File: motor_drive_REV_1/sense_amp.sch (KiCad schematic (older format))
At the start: 6 parts, among them U9 AD8418ABRMZ-RL

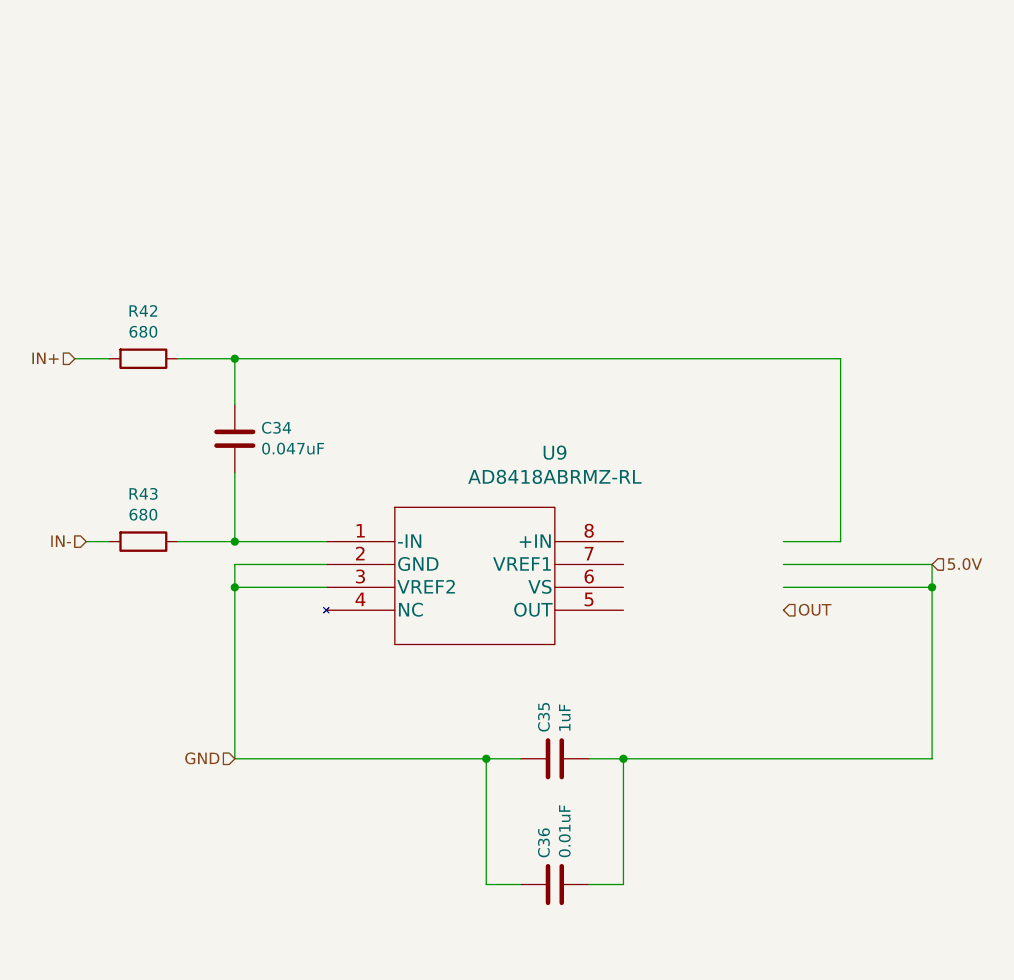
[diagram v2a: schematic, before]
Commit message: working on adding thermistors but encountered too many hierarchicaly copies bug
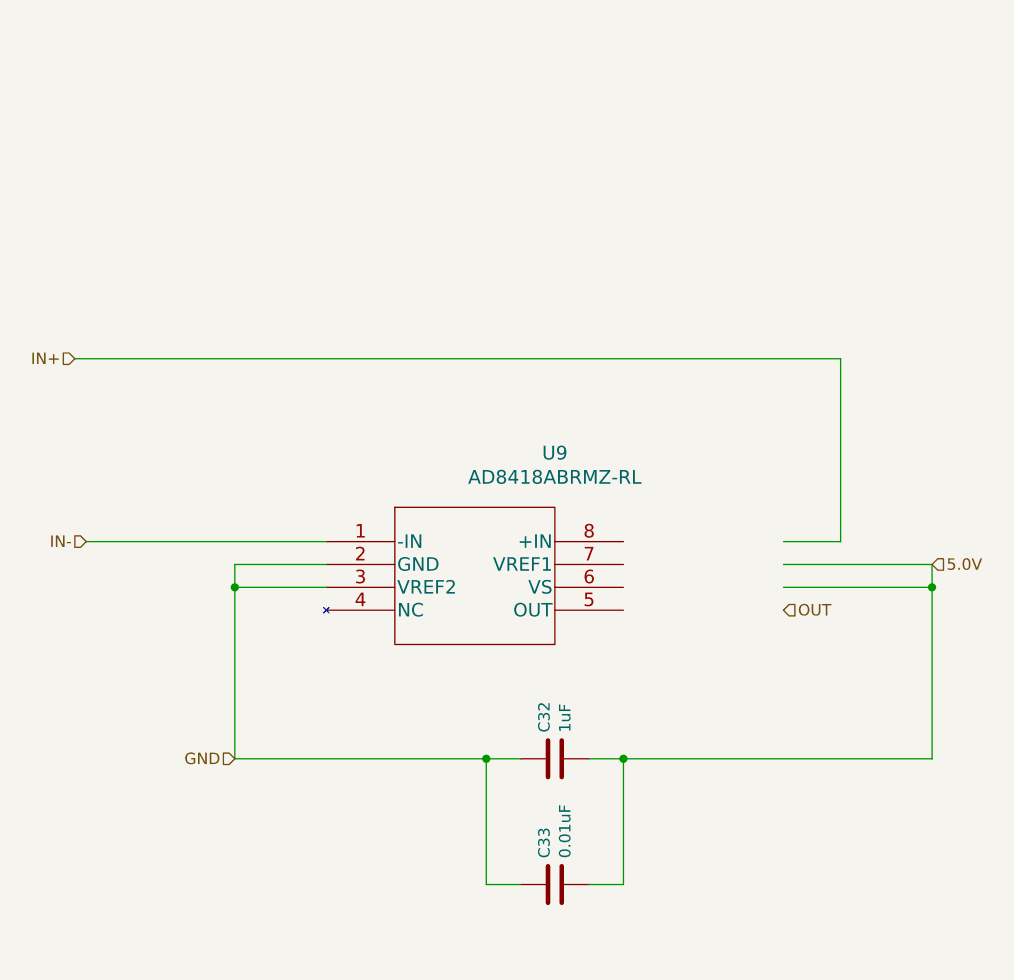
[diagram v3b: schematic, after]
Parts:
- removed C1: 0.047uF, motor_drive_footprints:C_0603_1608Metric, symbol motor_drive:C
- removed R10, R11: 680, motor_drive_footprints:C_0603_1608Metric, symbol motor_drive:R
- renumbered C35 to C32, C36 to C33
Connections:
- wire segments 26 -> 20
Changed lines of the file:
@@
 $Descr A4 11693 8268
 encoding utf-8
-Sheet 14 14
+Sheet 5 14
 Title ""
 Date ""
@@
 AR Path="/5E285F18/5E25CC80" Ref="C?"  Part="1"
 AR Path="/5E286BCF/5E25CC80" Ref="C?"  Part="1"
-AR Path="/5E291A12/5E25CC80" Ref="C35"  Part="1"
-AR Path="/5E2938C8/5E25CC80" Ref="C2"  Part="1"
+AR Path="/5E291A12/5E25CC80" Ref="C32"  Part="1"
+AR Path="/5E2938C8/5E25CC80" Ref="C3"  Part="1"
 AR Path="/5E295828/5E25CC80" Ref="C5"  Part="1"
 AR Path="/5E2E3D6E/5E25CC80" Ref="C?"  Part="1"
 AR Path="/5E2E5BBE/5E25CC80" Ref="C?"  Part="1"
 AR Path="/5E2E7F62/5E25CC80" Ref="C?"  Part="1"
-AR Path="/5E336639/5E25CC80" Ref="C8"  Part="1"
-AR Path="/5E33A08D/5E25CC80" Ref="C11"  Part="1"
+AR Path="/5E336639/5E25CC80" Ref="C7"  Part="1"
+AR Path="/5E33A08D/5E25CC80" Ref="C9"  Part="1"
 AR Path="/5E33E36D/5E25CC80" Ref="C?"  Part="1"
-F 0 "C35" H 5615 4496 50  0000 L CNN
+F 0 "C32" H 5615 4496 50  0000 L CNN
 F 1 "1uF" H 5615 4405 50  0000 L CNN
 F 2 "motor_drive_footprints:C_0603_1608Metric" H 5538 4300 50  0001 C CNN
@@
 AR Path="/5E285F18/5E3A2D2D" Ref="C?"  Part="1"
 AR Path="/5E286BCF/5E3A2D2D" Ref="C?"  Part="1"
-AR Path="/5E291A12/5E3A2D2D" Ref="C36"  Part="1"
-AR Path="/5E2938C8/5E3A2D2D" Ref="C3"  Part="1"
+AR Path="/5E291A12/5E3A2D2D" Ref="C33"  Part="1"
+AR Path="/5E2938C8/5E3A2D2D" Ref="C4"  Part="1"
 AR Path="/5E295828/5E3A2D2D" Ref="C6"  Part="1"
 AR Path="/5E2E3D6E/5E3A2D2D" Ref="C?"  Part="1"
 AR Path="/5E2E5BBE/5E3A2D2D" Ref="C?"  Part="1"
 AR Path="/5E2E7F62/5E3A2D2D" Ref="C?"  Part="1"
-AR Path="/5E336639/5E3A2D2D" Ref="C9"  Part="1"
-AR Path="/5E33A08D/5E3A2D2D" Ref="C12"  Part="1"
+AR Path="/5E336639/5E3A2D2D" Ref="C8"  Part="1"
+AR Path="/5E33A08D/5E3A2D2D" Ref="C10"  Part="1"
 AR Path="/5E33E36D/5E3A2D2D" Ref="C?"  Part="1"
-F 0 "C36" H 5615 5046 50  0000 L CNN
+F 0 "C33" H 5615 5046 50  0000 L CNN
 F 1 "0.01uF" H 5615 4955 50  0000 L CNN
 F 2 "motor_drive_footprints:C_0603_1608Metric" H 5538 4850 50  0001 C CNN
@@
 Text HLabel 3450 3500 0    50   Input ~ 0
 IN-
-$Comp
-L motor_drive:R R?
-U 1 1 5E3B6CAC
-P 3700 2700
-AR Path="/5E26944C/5E3B6CAC" Ref="R?"  Part="1"
-AR Path="/5E3B6CAC" Ref="R?"  Part="1"
-AR Path="/5E334D58/5E3B6CAC" Ref="R?"  Part="1"
-AR Path="/5E2938C8/5E3B6CAC" Ref="R10"  Part="1"
-AR Path="/5E295828/5E3B6CAC" Ref="R12"  Part="1"
-AR Path="/5E336639/5E3B6CAC" Ref="R14"  Part="1"
-AR Path="/5E33A08D/5E3B6CAC" Ref="R16"  Part="1"
-AR Path="/5E291A12/5E3B6CAC" Ref="R42"  Part="1"
-F 0 "R42" V 3493 2700 50  0000 C CNN
-F 1 "680" V 3584 2700 50  0000 C CNN
-F 2 "motor_drive_footprints:C_0603_1608Metric" V 3630 2700 50  0001 C CNN
-F 3 "~" H 3700 2700 50  0001 C CNN
-	1    3700 2700
-	0    1    1    0
-$EndComp
-$Comp
-L motor_drive:C C?
-U 1 1 5E3B79F8
-P 4100 3050
-AR Path="/5E38D632/5E3B79F8" Ref="C?"  Part="1"
-AR Path="/5E334D58/5E3B79F8" Ref="C?"  Part="1"
-AR Path="/5E2938C8/5E3B79F8" Ref="C1"  Part="1"
-AR Path="/5E295828/5E3B79F8" Ref="C4"  Part="1"
-AR Path="/5E336639/5E3B79F8" Ref="C7"  Part="1"
-AR Path="/5E33A08D/5E3B79F8" Ref="C10"  Part="1"
-AR Path="/5E291A12/5E3B79F8" Ref="C34"  Part="1"
-F 0 "C34" H 4215 3096 50  0000 L CNN
-F 1 "0.047uF" H 4215 3005 50  0000 L CNN
-F 2 "motor_drive_footprints:C_0603_1608Metric" H 4138 2900 50  0001 C CNN
-F 3 "~" H 4100 3050 50  0001 C CNN
-	1    4100 3050
-	1    0    0    -1
-$EndComp
-Wire Wire Line
-	3400 2700 3550 2700
-Wire Wire Line
-	3850 2700 4100 2700
-Wire Wire Line
-	4100 2700 6750 2700
 Wire Wire Line
 	6750 2700 6750 3500
-Connection ~ 4100 2700
 Wire Wire Line
-	4100 2700 4100 2900
+	3400 2700 6750 2700
 Wire Wire Line
-	4100 3200 4100 3500
-Wire Wire Line
-	4100 3500 4500 3500
-$Comp
-L motor_drive:R R?
-U 1 1 5E394586
-P 3700 3500
-AR Path="/5E26944C/5E394586" Ref="R?"  Part="1"
-AR Path="/5E394586" Ref="R?"  Part="1"
-AR Path="/5E334D58/5E394586" Ref="R?"  Part="1"
-AR Path="/5E2938C8/5E394586" Ref="R11"  Part="1"
-AR Path="/5E295828/5E394586" Ref="R13"  Part="1"
-AR Path="/5E336639/5E394586" Ref="R15"  Part="1"
-AR Path="/5E33A08D/5E394586" Ref="R17"  Part="1"
-AR Path="/5E291A12/5E394586" Ref="R43"  Part="1"
-F 0 "R43" V 3493 3500 50  0000 C CNN
-F 1 "680" V 3584 3500 50  0000 C CNN
-F 2 "motor_drive_footprints:C_0603_1608Metric" V 3630 3500 50  0001 C CNN
-F 3 "~" H 3700 3500 50  0001 C CNN
-	1    3700 3500
-	0    1    1    0
-$EndComp
-Wire Wire Line
-	3850 3500 4100 3500
-Connection ~ 4100 3500
-Wire Wire Line
-	3550 3500 3450 3500
+	3450 3500 4500 3500
 $EndSCHEMATC

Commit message: started layout
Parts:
- renumbered C32 to C41, C33 to C42
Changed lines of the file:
@@
 $Descr A4 11693 8268
 encoding utf-8
-Sheet 5 14
+Sheet 6 16
 Title ""
 Date ""
@@
 AR Path="/5E33A08D/5E259F13" Ref="U4"  Part="1"
 AR Path="/5E33E36D/5E259F13" Ref="U?"  Part="1"
-F 0 "U9" H 5500 3887 60  0000 C CNN
+F 0 "U2" H 5500 3887 60  0000 C CNN
 F 1 "AD8418ABRMZ-RL" H 5500 3781 60  0000 C CNN
 F 2 "motor_drive_footprints:AD8418ABRMZ-RL" H 5500 3740 60  0001 C CNN
@@
 AR Path="/5E285F18/5E25CC80" Ref="C?"  Part="1"
 AR Path="/5E286BCF/5E25CC80" Ref="C?"  Part="1"
-AR Path="/5E291A12/5E25CC80" Ref="C32"  Part="1"
-AR Path="/5E2938C8/5E25CC80" Ref="C3"  Part="1"
-AR Path="/5E295828/5E25CC80" Ref="C5"  Part="1"
+AR Path="/5E291A12/5E25CC80" Ref="C41"  Part="1"
+AR Path="/5E2938C8/5E25CC80" Ref="C1"  Part="1"
+AR Path="/5E295828/5E25CC80" Ref="C3"  Part="1"
 AR Path="/5E2E3D6E/5E25CC80" Ref="C?"  Part="1"
 AR Path="/5E2E5BBE/5E25CC80" Ref="C?"  Part="1"
 AR Path="/5E2E7F62/5E25CC80" Ref="C?"  Part="1"
-AR Path="/5E336639/5E25CC80" Ref="C7"  Part="1"
-AR Path="/5E33A08D/5E25CC80" Ref="C9"  Part="1"
+AR Path="/5E336639/5E25CC80" Ref="C5"  Part="1"
+AR Path="/5E33A08D/5E25CC80" Ref="C7"  Part="1"
 AR Path="/5E33E36D/5E25CC80" Ref="C?"  Part="1"
-F 0 "C32" H 5615 4496 50  0000 L CNN
+F 0 "C3" H 5615 4496 50  0000 L CNN
 F 1 "1uF" H 5615 4405 50  0000 L CNN
 F 2 "motor_drive_footprints:C_0603_1608Metric" H 5538 4300 50  0001 C CNN
@@
 AR Path="/5E285F18/5E3A2D2D" Ref="C?"  Part="1"
 AR Path="/5E286BCF/5E3A2D2D" Ref="C?"  Part="1"
-AR Path="/5E291A12/5E3A2D2D" Ref="C33"  Part="1"
-AR Path="/5E2938C8/5E3A2D2D" Ref="C4"  Part="1"
-AR Path="/5E295828/5E3A2D2D" Ref="C6"  Part="1"
+AR Path="/5E291A12/5E3A2D2D" Ref="C42"  Part="1"
+AR Path="/5E2938C8/5E3A2D2D" Ref="C2"  Part="1"
+AR Path="/5E295828/5E3A2D2D" Ref="C4"  Part="1"
 AR Path="/5E2E3D6E/5E3A2D2D" Ref="C?"  Part="1"
 AR Path="/5E2E5BBE/5E3A2D2D" Ref="C?"  Part="1"
 AR Path="/5E2E7F62/5E3A2D2D" Ref="C?"  Part="1"
-AR Path="/5E336639/5E3A2D2D" Ref="C8"  Part="1"
-AR Path="/5E33A08D/5E3A2D2D" Ref="C10"  Part="1"
+AR Path="/5E336639/5E3A2D2D" Ref="C6"  Part="1"
+AR Path="/5E33A08D/5E3A2D2D" Ref="C8"  Part="1"
 AR Path="/5E33E36D/5E3A2D2D" Ref="C?"  Part="1"
-F 0 "C33" H 5615 5046 50  0000 L CNN
+F 0 "C4" H 5615 5046 50  0000 L CNN
 F 1 "0.01uF" H 5615 4955 50  0000 L CNN
 F 2 "motor_drive_footprints:C_0603_1608Metric" H 5538 4850 50  0001 C CNN

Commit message: layout
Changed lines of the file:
@@
 $Descr A4 11693 8268
 encoding utf-8
-Sheet 6 16
+Sheet 14 16
 Title ""
 Date ""
@@
 AR Path="/5E33A08D/5E259F13" Ref="U4"  Part="1"
 AR Path="/5E33E36D/5E259F13" Ref="U?"  Part="1"
-F 0 "U2" H 5500 3887 60  0000 C CNN
+F 0 "U9" H 5500 3887 60  0000 C CNN
 F 1 "AD8418ABRMZ-RL" H 5500 3781 60  0000 C CNN
 F 2 "motor_drive_footprints:AD8418ABRMZ-RL" H 5500 3740 60  0001 C CNN
@@
 AR Path="/5E33A08D/5E25CC80" Ref="C7"  Part="1"
 AR Path="/5E33E36D/5E25CC80" Ref="C?"  Part="1"
-F 0 "C3" H 5615 4496 50  0000 L CNN
+F 0 "C41" H 5615 4496 50  0000 L CNN
 F 1 "1uF" H 5615 4405 50  0000 L CNN
 F 2 "motor_drive_footprints:C_0603_1608Metric" H 5538 4300 50  0001 C CNN
@@
 AR Path="/5E33A08D/5E3A2D2D" Ref="C8"  Part="1"
 AR Path="/5E33E36D/5E3A2D2D" Ref="C?"  Part="1"
-F 0 "C4" H 5615 5046 50  0000 L CNN
+F 0 "C42" H 5615 5046 50  0000 L CNN
 F 1 "0.01uF" H 5615 4955 50  0000 L CNN
 F 2 "motor_drive_footprints:C_0603_1608Metric" H 5538 4850 50  0001 C CNN

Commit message: layout
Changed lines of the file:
@@
 $Descr A4 11693 8268
 encoding utf-8
-Sheet 14 16
+Sheet 6 16
 Title ""
 Date ""
@@
 AR Path="/5E33A08D/5E259F13" Ref="U4"  Part="1"
 AR Path="/5E33E36D/5E259F13" Ref="U?"  Part="1"
-F 0 "U9" H 5500 3887 60  0000 C CNN
+F 0 "U2" H 5500 3887 60  0000 C CNN
 F 1 "AD8418ABRMZ-RL" H 5500 3781 60  0000 C CNN
 F 2 "motor_drive_footprints:AD8418ABRMZ-RL" H 5500 3740 60  0001 C CNN
@@
 AR Path="/5E33A08D/5E25CC80" Ref="C7"  Part="1"
 AR Path="/5E33E36D/5E25CC80" Ref="C?"  Part="1"
-F 0 "C41" H 5615 4496 50  0000 L CNN
+F 0 "C3" H 5615 4496 50  0000 L CNN
 F 1 "1uF" H 5615 4405 50  0000 L CNN
 F 2 "motor_drive_footprints:C_0603_1608Metric" H 5538 4300 50  0001 C CNN
@@
 AR Path="/5E33A08D/5E3A2D2D" Ref="C8"  Part="1"
 AR Path="/5E33E36D/5E3A2D2D" Ref="C?"  Part="1"
-F 0 "C42" H 5615 5046 50  0000 L CNN
+F 0 "C4" H 5615 5046 50  0000 L CNN
 F 1 "0.01uF" H 5615 4955 50  0000 L CNN
 F 2 "motor_drive_footprints:C_0603_1608Metric" H 5538 4850 50  0001 C CNN

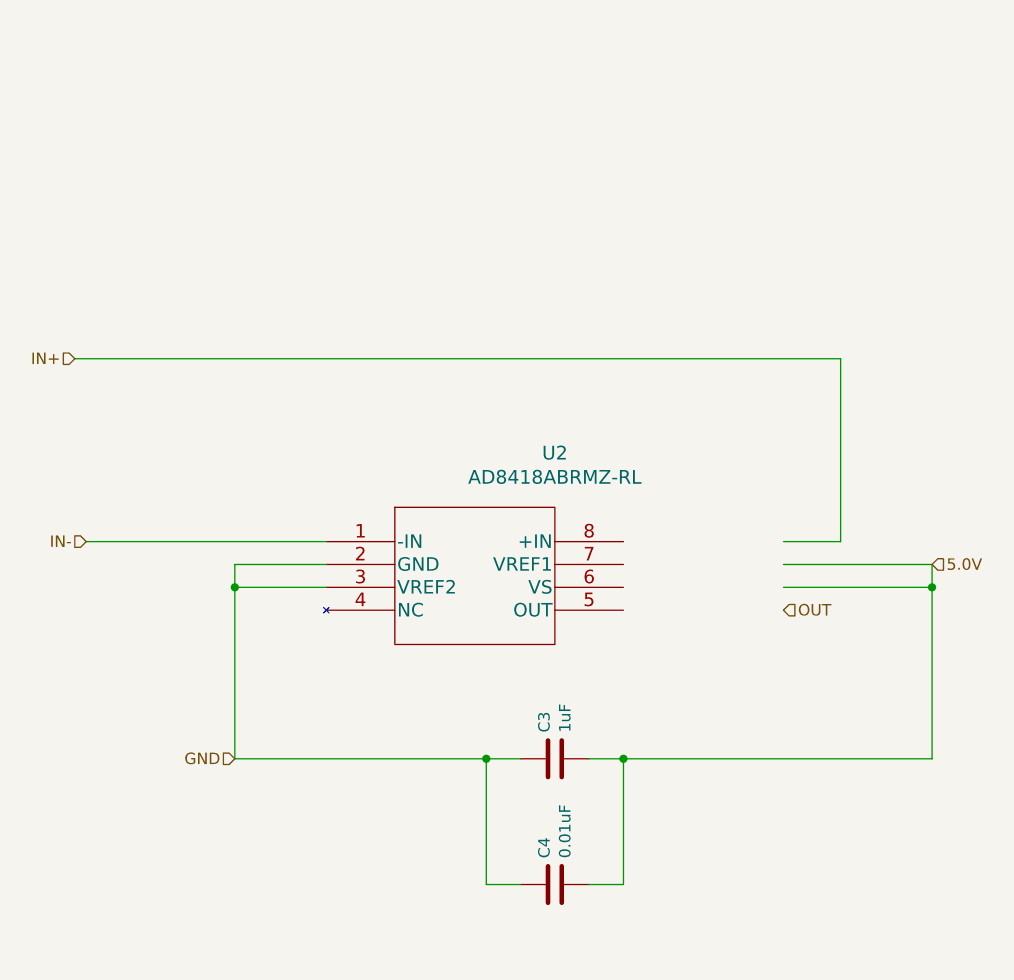
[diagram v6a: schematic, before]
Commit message: gate drive rework and schematic re-organization
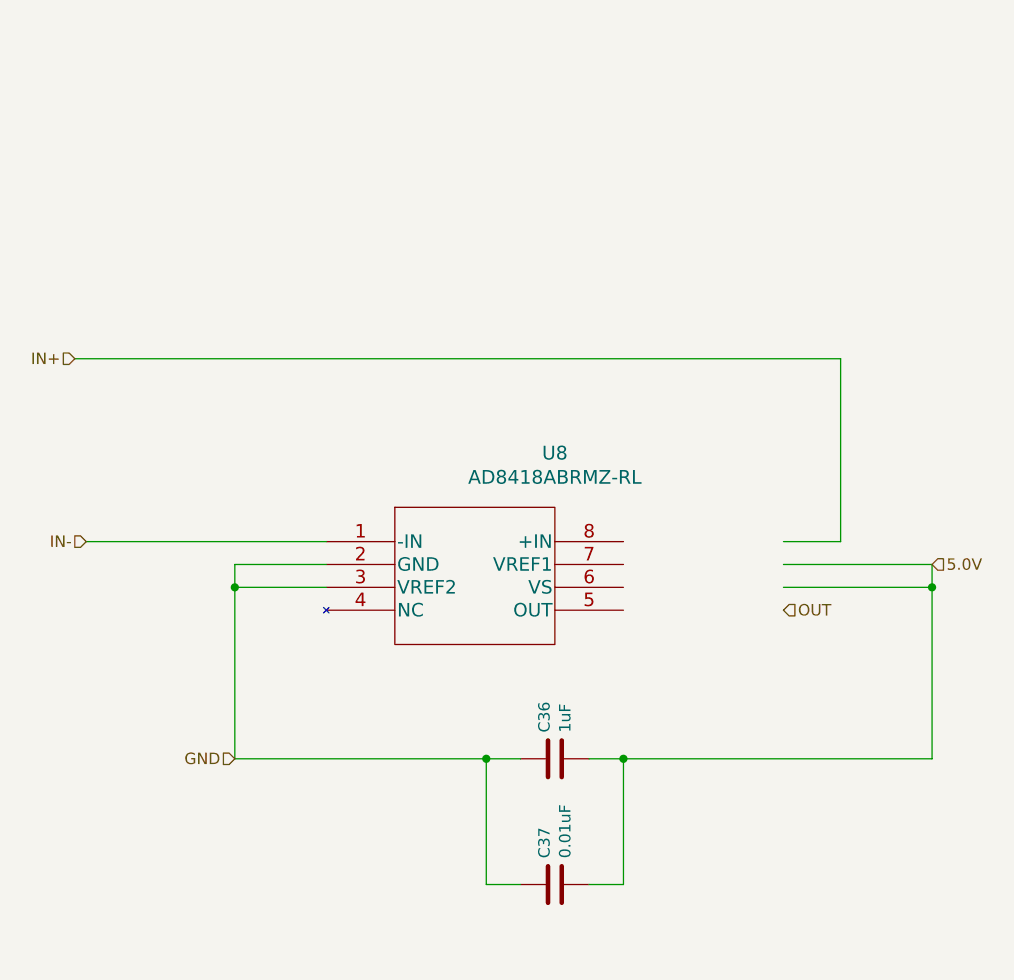
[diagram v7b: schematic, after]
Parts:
- renumbered C41 to C36, C42 to C37, U9 to U8
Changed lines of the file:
@@
 $Descr A4 11693 8268
 encoding utf-8
-Sheet 6 16
+Sheet 10 15
 Title ""
 Date ""
@@
 IN+
 $Comp
-L motor_drive:AD8418ABRMZ-RL U9
+L motor_drive:AD8418ABRMZ-RL U8
 U 1 1 5E259F13
 P 4500 3500
-AR Path="/5E291A12/5E259F13" Ref="U9"  Part="1"
+AR Path="/5E291A12/5E259F13" Ref="U8"  Part="1"
 AR Path="/5E2938C8/5E259F13" Ref="U1"  Part="1"
 AR Path="/5E295828/5E259F13" Ref="U2"  Part="1"
@@
 AR Path="/5E33A08D/5E259F13" Ref="U4"  Part="1"
 AR Path="/5E33E36D/5E259F13" Ref="U?"  Part="1"
-F 0 "U2" H 5500 3887 60  0000 C CNN
+F 0 "U8" H 5500 3887 60  0000 C CNN
 F 1 "AD8418ABRMZ-RL" H 5500 3781 60  0000 C CNN
 F 2 "motor_drive_footprints:AD8418ABRMZ-RL" H 5500 3740 60  0001 C CNN
@@
 AR Path="/5E285F18/5E25CC80" Ref="C?"  Part="1"
 AR Path="/5E286BCF/5E25CC80" Ref="C?"  Part="1"
-AR Path="/5E291A12/5E25CC80" Ref="C41"  Part="1"
+AR Path="/5E291A12/5E25CC80" Ref="C36"  Part="1"
 AR Path="/5E2938C8/5E25CC80" Ref="C1"  Part="1"
 AR Path="/5E295828/5E25CC80" Ref="C3"  Part="1"
@@
 AR Path="/5E33A08D/5E25CC80" Ref="C7"  Part="1"
 AR Path="/5E33E36D/5E25CC80" Ref="C?"  Part="1"
-F 0 "C3" H 5615 4496 50  0000 L CNN
+F 0 "C36" H 5615 4496 50  0000 L CNN
 F 1 "1uF" H 5615 4405 50  0000 L CNN
 F 2 "motor_drive_footprints:C_0603_1608Metric" H 5538 4300 50  0001 C CNN
@@
 AR Path="/5E285F18/5E3A2D2D" Ref="C?"  Part="1"
 AR Path="/5E286BCF/5E3A2D2D" Ref="C?"  Part="1"
-AR Path="/5E291A12/5E3A2D2D" Ref="C42"  Part="1"
+AR Path="/5E291A12/5E3A2D2D" Ref="C37"  Part="1"
 AR Path="/5E2938C8/5E3A2D2D" Ref="C2"  Part="1"
 AR Path="/5E295828/5E3A2D2D" Ref="C4"  Part="1"
@@
 AR Path="/5E33A08D/5E3A2D2D" Ref="C8"  Part="1"
 AR Path="/5E33E36D/5E3A2D2D" Ref="C?"  Part="1"
-F 0 "C4" H 5615 5046 50  0000 L CNN
+F 0 "C37" H 5615 5046 50  0000 L CNN
 F 1 "0.01uF" H 5615 4955 50  0000 L CNN
 F 2 "motor_drive_footprints:C_0603_1608Metric" H 5538 4850 50  0001 C CNN
